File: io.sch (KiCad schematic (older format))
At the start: 10 parts, among them J2 Feather_BOT, J3 Feather_TOP, Q1 MMBT3904, SW1 USER

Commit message: Add digikey pn's to schematic, update BOM
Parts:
- C4: Digikey (none) -> 490-14603-1-ND
- D2: Digikey (none) -> 160-1447-1-ND
- J2, J3: Digikey (none) -> DNP; LCSC (none) -> DNP
- Q1: Digikey (none) -> MMBT3904-FDICT-ND
- R10: Digikey (none) -> 311-330LRCT-ND
- R7: Digikey (none) -> 311-1.00KLRCT-ND
- R8, R9: Digikey (none) -> 311-10.0KLRTR-ND
- SW1: Digikey (none) -> EG2531CT-ND
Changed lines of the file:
@@
 F 2 "Connector_PinHeader_2.54mm:PinHeader_1x12_P2.54mm_Vertical" H 5800 2950 50  0001 C CNN
 F 3 "~" H 5800 2950 50  0001 C CNN
+F 4 "DNP" V 5800 2950 50  0001 C CNN "LCSC"
+F 5 "DNP" V 5800 2950 50  0001 C CNN "Digikey"
 	1    5800 2950
 	0    -1   -1   0
@@
 F 2 "Connector_PinHeader_2.54mm:PinHeader_1x16_P2.54mm_Vertical" H 5600 5200 50  0001 C CNN
 F 3 "~" H 5600 5200 50  0001 C CNN
+F 4 "DNP" V 5600 5200 50  0001 C CNN "LCSC"
+F 5 "DNP" V 5600 5200 50  0001 C CNN "Digikey"
 	1    5600 5200
 	0    -1   1    0
@@
 F 3 "~" H 8450 1450 50  0001 C CNN
 F 4 "C25744" H 8450 1450 50  0001 C CNN "LCSC"
+F 5 "311-10.0KLRTR-ND" H 8450 1450 50  0001 C CNN "Digikey"
 	1    8450 1450
 	1    0    0    -1
@@
 F 3 "~" H 8450 2150 50  0001 C CNN
 F 4 "C1525" H 8450 2150 50  0001 C CNN "LCSC"
+F 5 "490-14603-1-ND" H 8450 2150 50  0001 C CNN "Digikey"
 	1    8450 2150
 	1    0    0    -1
@@
 F 3 "~" H 8950 2400 50  0001 C CNN
 F 4 "C318884" V 8950 2200 50  0001 C CNN "LCSC"
+F 5 "EG2531CT-ND" V 8950 2200 50  0001 C CNN "Digikey"
 	1    8950 2200
 	0    1    1    0
@@
 F 3 "~" H 8500 4650 50  0001 C CNN
 F 4 "C20526" H 8500 4650 50  0001 C CNN "LCSC"
+F 5 "MMBT3904-FDICT-ND" H 8500 4650 50  0001 C CNN "Digikey"
 	1    8500 4650
 	1    0    0    -1
@@
 F 3 "~" H 8050 4650 50  0001 C CNN
 F 4 "C11702" V 8050 4650 50  0001 C CNN "LCSC"
+F 5 "311-1.00KLRCT-ND" V 8050 4650 50  0001 C CNN "Digikey"
 	1    8050 4650
 	0    1    1    0
@@
 F 3 "~" H 8600 4200 50  0001 C CNN
 F 4 "C25104" H 8600 4200 50  0001 C CNN "LCSC"
+F 5 "311-330LRCT-ND" H 8600 4200 50  0001 C CNN "Digikey"
 	1    8600 4200
 	-1   0    0    1
@@
 F 3 "~" H 8600 3800 50  0001 C CNN
 F 4 "C72043" V 8600 3800 50  0001 C CNN "LCSC"
+F 5 "160-1447-1-ND" V 8600 3800 50  0001 C CNN "Digikey"
 	1    8600 3800
 	0    -1   -1   0
@@
 F 3 "~" H 8300 5150 50  0001 C CNN
 F 4 "C25744" V 8300 5150 50  0001 C CNN "LCSC"
+F 5 "311-10.0KLRTR-ND" V 8300 5150 50  0001 C CNN "Digikey"
 	1    8300 5150
 	0    1    1    0
@@
 NoConn ~ 5100 5000
 $Comp
-L Graphic:Logo_Open_Hardware_Small #LOGO?
+L Graphic:Logo_Open_Hardware_Small #LOGO2
 U 1 1 5DD33969
 P 10950 6900
-F 0 "#LOGO?" H 10950 7175 50  0001 C CNN
+F 0 "#LOGO2" H 10950 7175 50  0001 C CNN
 F 1 "Logo_Open_Hardware_Small" H 10950 6675 50  0001 C CNN
 F 2 "" H 10950 6900 50  0001 C CNN
@@
 $EndComp
 $Comp
-L Graphic:SYM_Radio_Waves_Large #SYM?
+L Graphic:SYM_Radio_Waves_Large #SYM2
 U 1 1 5DD3396F
 P 10400 6850
-F 0 "#SYM?" H 10400 7050 50  0001 C CNN
+F 0 "#SYM2" H 10400 7050 50  0001 C CNN
 F 1 "SYM_Radio_Waves_Large" H 10400 6600 50  0001 C CNN
 F 2 "" H 10400 6650 50  0001 C CNN

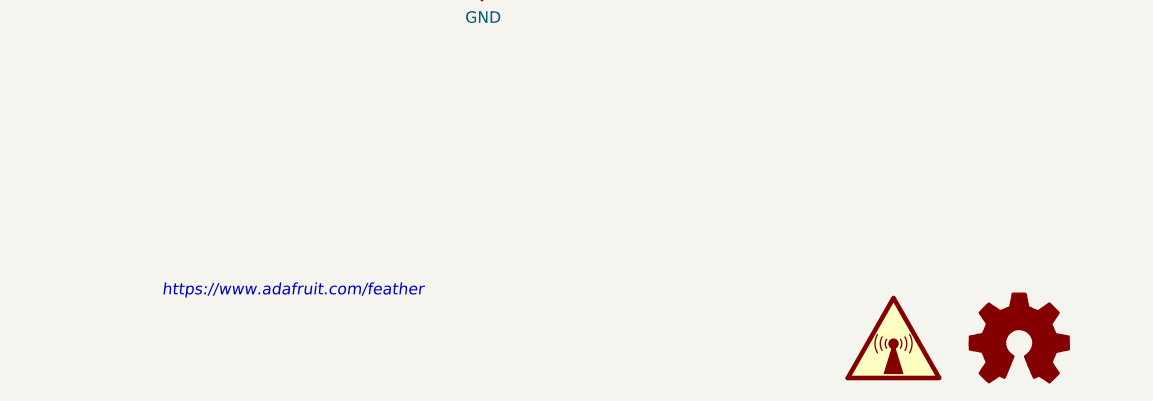
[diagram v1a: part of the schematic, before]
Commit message: PCB REV C0 * Make U8 footprint capable of crypto and fram device * Minor updates to schematic * Minor updates to doc prints * Update bot silk to REV C0
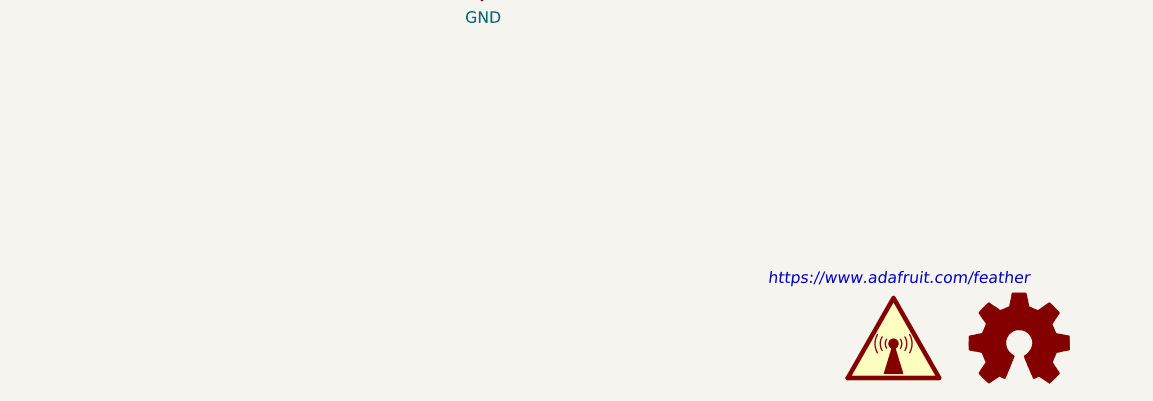
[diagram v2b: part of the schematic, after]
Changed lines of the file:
@@
 EndData
 $EndBitmap
-Text Notes 7200 6700 0    50   Italic 0
+Text Notes 9850 6650 0    50   Italic 0
 https://www.adafruit.com/feather
 $Bitmap
